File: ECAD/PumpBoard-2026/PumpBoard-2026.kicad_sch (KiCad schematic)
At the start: 22 parts, among them J1 Conn_01x04, J3 CON_EV, J4 CON_PUMP, Q1 AO3400A, Q2 AO3400A

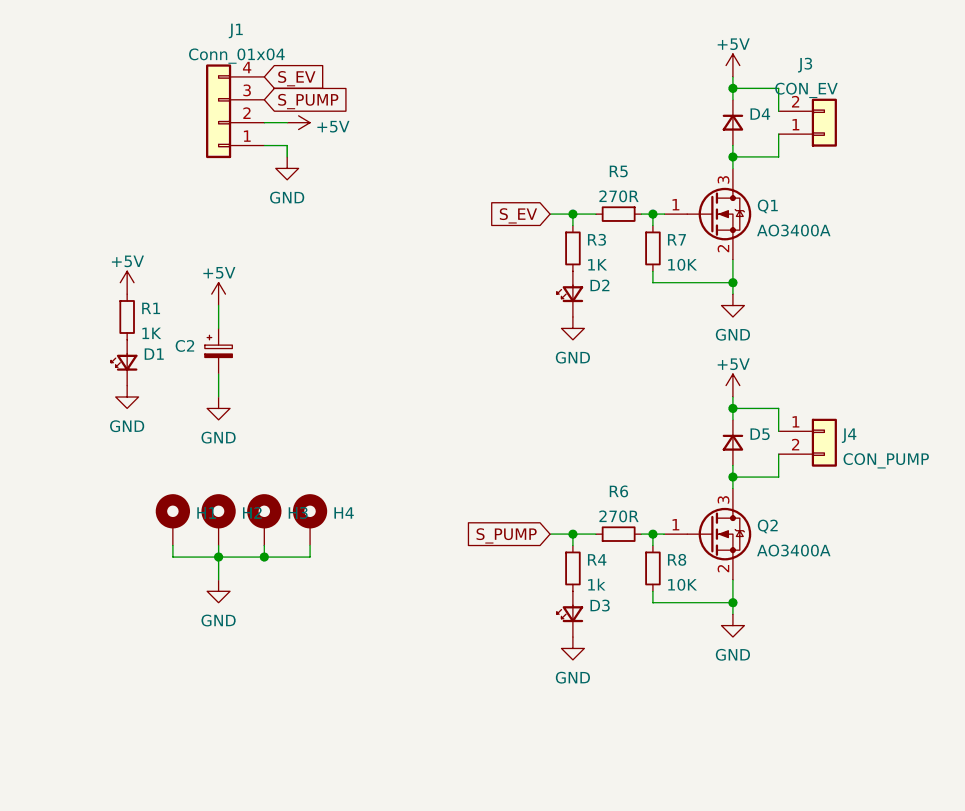
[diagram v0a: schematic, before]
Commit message: change capacitor size
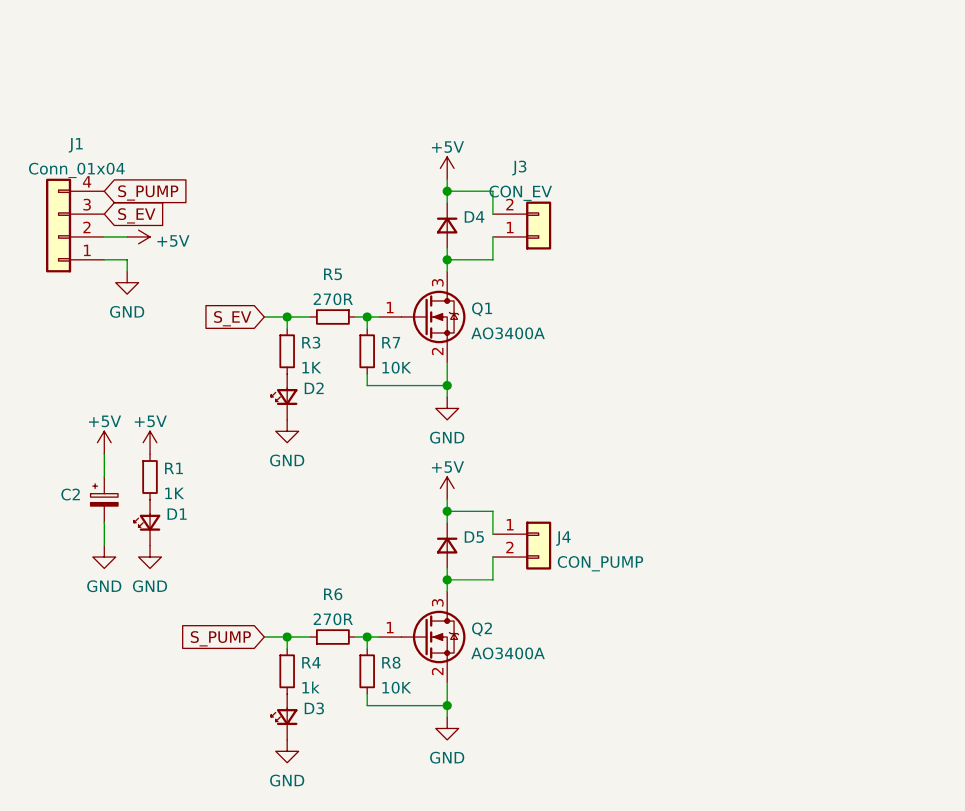
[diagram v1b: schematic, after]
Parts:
- removed H1, H2, H3, H4: MountingHole_Pad, MountingHole:MountingHole_3.2mm_M3_Pad_Via, symbol Mechanical:MountingHole_Pad
- C2: footprint Capacitor_THT:CP_Radial_D10.0mm_P5.00mm -> Capacitor_THT:CP_Radial_D8.0mm_P5.00mm
- J3: footprint BarbaLib:MiniEV -> Connector_Molex:Molex_KK-254_AE-6410-02A_1x02_P2.54mm_Vertical
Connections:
- net S_EV: now also J1.3 (Pin_3); no longer J1.4 (Pin_4)
- net S_PUMP: now also J1.4 (Pin_4); no longer J1.3 (Pin_3)
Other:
- moved on the sheet: C2, D1, D2, D3, D4, D5, J1, J3, J4, Q1, Q2, R1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
